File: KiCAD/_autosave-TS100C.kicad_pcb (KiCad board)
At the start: 4 copper layers, 84 x 10 mm, 62 parts, among them J1 USB_C_Receptacle_USB2.0, J2 OLED_64x32, J3 A, J4 B, J5 DNP, P1 TC2030-CTX, Q1 SS8050, Q2 DMP3017SFG, SW1 key1, SW2 key2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

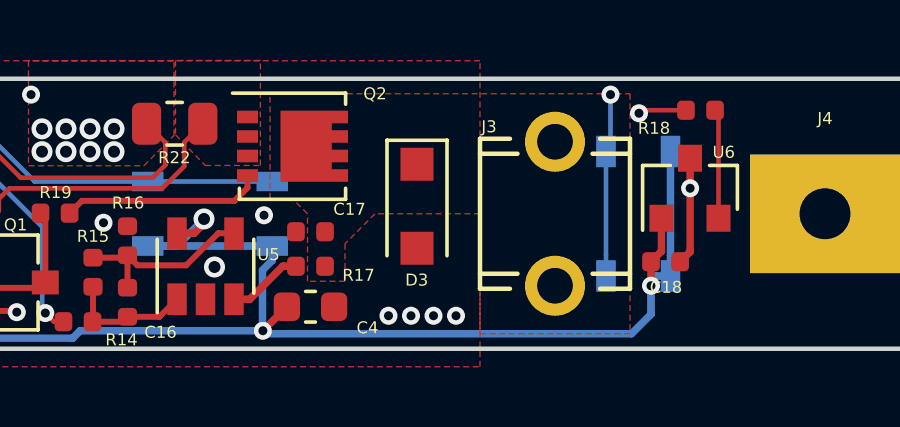
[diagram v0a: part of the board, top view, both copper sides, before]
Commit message: updated PCB+schematic to STUSB4500
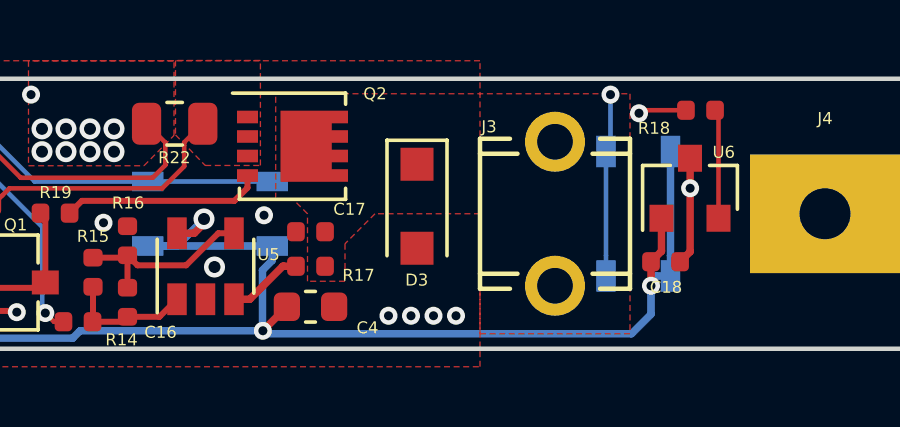
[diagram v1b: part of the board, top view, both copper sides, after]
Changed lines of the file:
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@@
       (usegerberadvancedattributes false)
       (creategerberjobfile false)
-      (excludeedgelayer true)
+      (excludeedgelayer false)
       (linewidth 0.100000)
       (plotframeref false)
@@
       (drillshape 0)
       (scaleselection 1)
-      (outputdirectory ""))
+      (outputdirectory "gerber/"))
   )
   (net 0 "")
@@
     (polygon
       (pts
-        (xy 142.5 84.5) (xy 142.5 81) (xy 154.5 81) (xy 154.5 89) (xy 149.5 89)
+        (xy 142.69 84.5) (xy 142.69 81) (xy 154.5 81) (xy 154.5 89) (xy 149.5 89)
         (xy 149.5 85) (xy 146 85) (xy 145 86) (xy 145 87.25) (xy 143.75 87.25)
         (xy 143.75 85) (xy 143.25 84.5)
